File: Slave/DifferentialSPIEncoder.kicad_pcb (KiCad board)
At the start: 2 copper layers, 52.3 x 42.7 mm, 31 parts, among them J1 Debug, J2 8P8C_LED_Shielded, U1 AS5047U, U3 SN65HVD06D, U4 SN65HVD06D, U5 SN65HVD06D

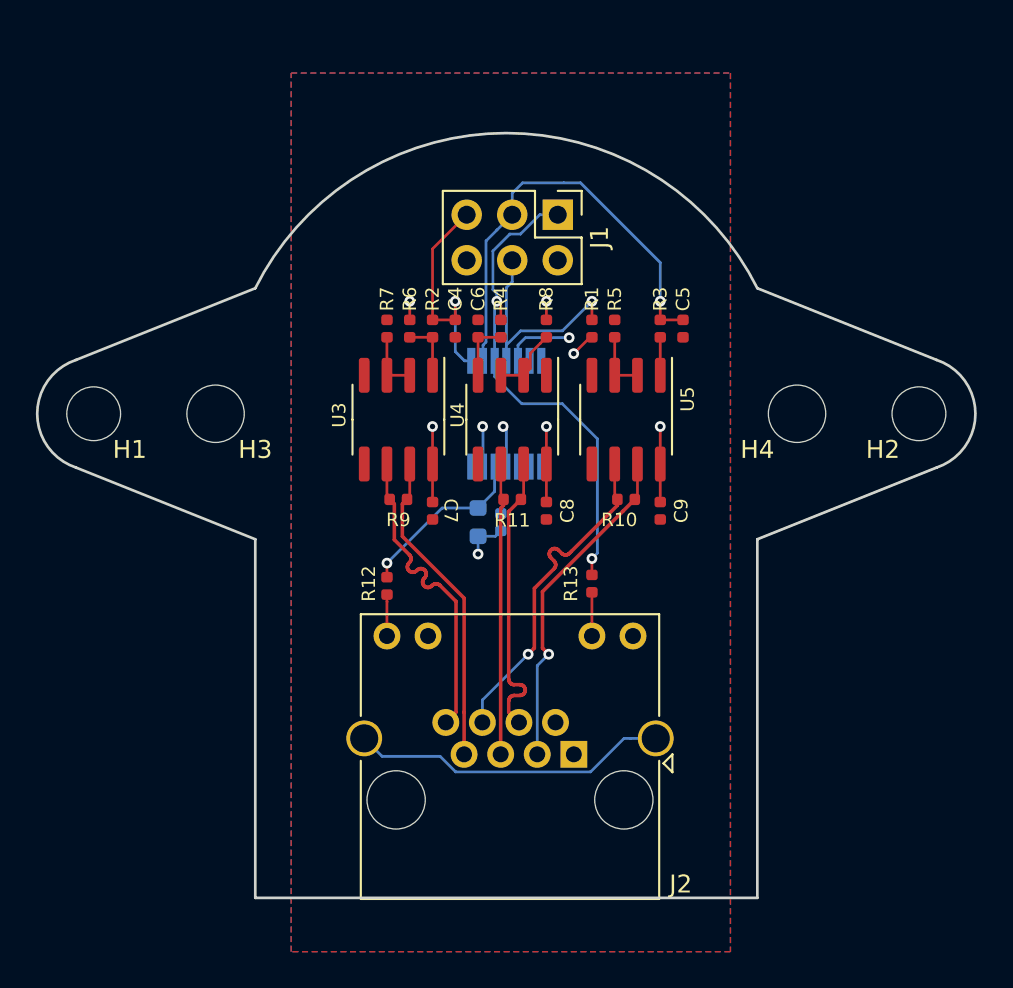
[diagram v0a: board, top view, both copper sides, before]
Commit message: Make a NEMA-17 compatible layout
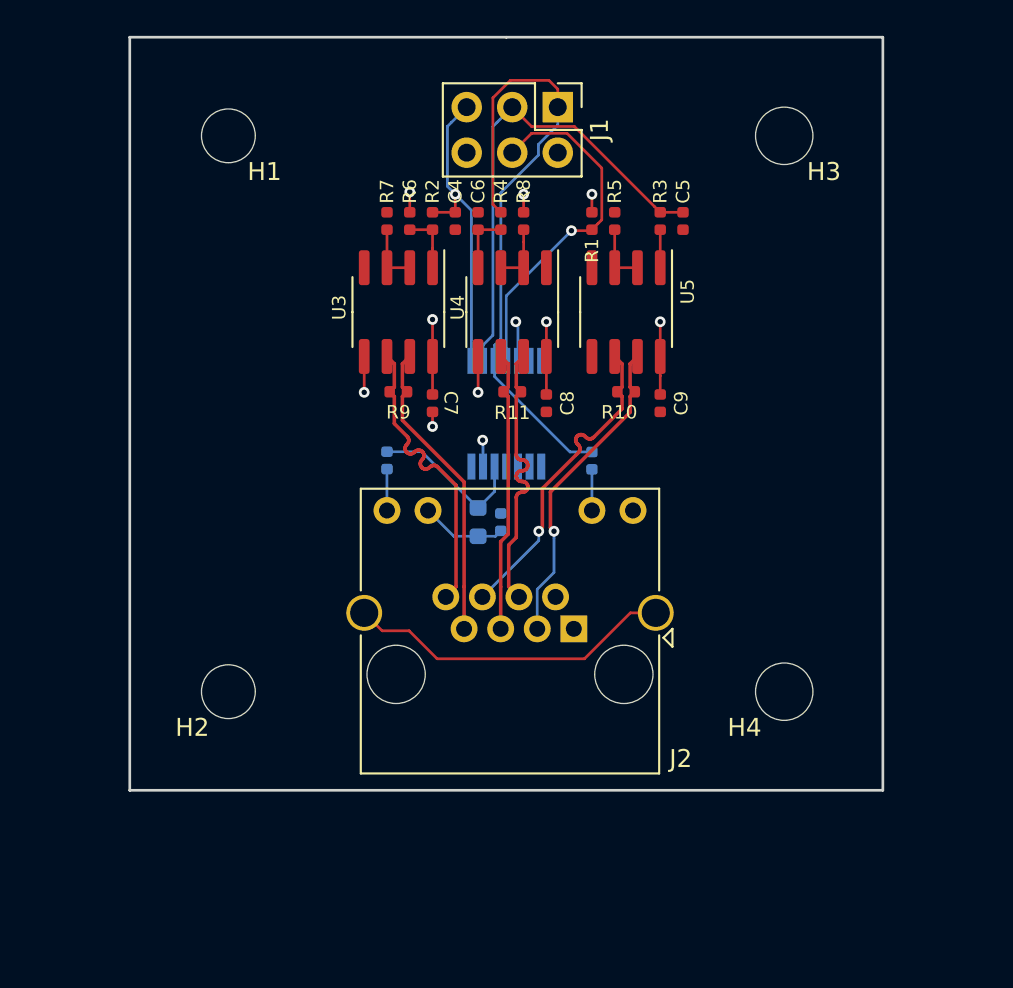
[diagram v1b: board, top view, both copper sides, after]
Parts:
- R12, R13: moved to B.Cu
- moved H2 41.5 mm to (84.5, 115.5)
- moved H3 35.3 mm to (115.5, 84.5)
- moved H1 17.2 mm to (84.5, 84.5)
- moved H4 15.5 mm to (115.5, 115.5)
- moved J2 7.00 mm to (103.8, 112.0)
- moved R12 7.00 mm to (93.3, 102.6)
- moved R13 6.86 mm to (104.8, 102.6)
- moved R8 6.13 mm to (101.0, 89.2)
- moved C4 6.00 mm to (97.2, 89.2)
- moved C5 6.00 mm to (109.9, 89.2)
- moved C6 6.00 mm to (98.4, 89.2)
- moved C7 6.00 mm to (95.9, 99.4)
- moved C8 6.00 mm to (102.2, 99.4)
- moved C9 6.00 mm to (108.6, 99.4)
- moved J1 6.00 mm to (102.9, 82.9)
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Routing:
- net MISO: track 27.6 -> 35.4 mm, vias 2 -> 0
- net /MOSI: track 12.6 -> 19.8 mm
- net GND: track 8.54 -> 13.3 mm, vias 3 -> 5
- net ~CSn: track 12.9 -> 17.4 mm
- net +5V: track 18.4 -> 15.4 mm, vias 7 -> 6
- net CLK: track 24.8 -> 26.8 mm, vias 1 -> 0
- net /CLK_+: track 18.8 -> 17.9 mm
- net /CLK_-: track 18.8 -> 17.9 mm
- net /CS_-: track 17.8 -> 17.0 mm
- net /CS_+: track 17.8 -> 17.0 mm
- net +3V3: track 9.83 -> 9.07 mm, vias 1 -> 0
- net Net-(J2-PadSH): track 17.8 -> 18.4 mm
- net /MISO_+: track 16.3 -> 15.7 mm
- net /MISO_-: track 16.3 -> 15.7 mm
- net Net-(R8-Pad2): track 3.92 -> 3.39 mm
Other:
- board size 52.3 x 42.7 mm -> 42 x 42 mm
